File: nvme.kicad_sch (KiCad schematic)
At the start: 18 parts, among them J3 Bus_M.2_Socket_M, U1 ASEK-32.768KHZ-L-R-T, U2 AP3441SHE-7B

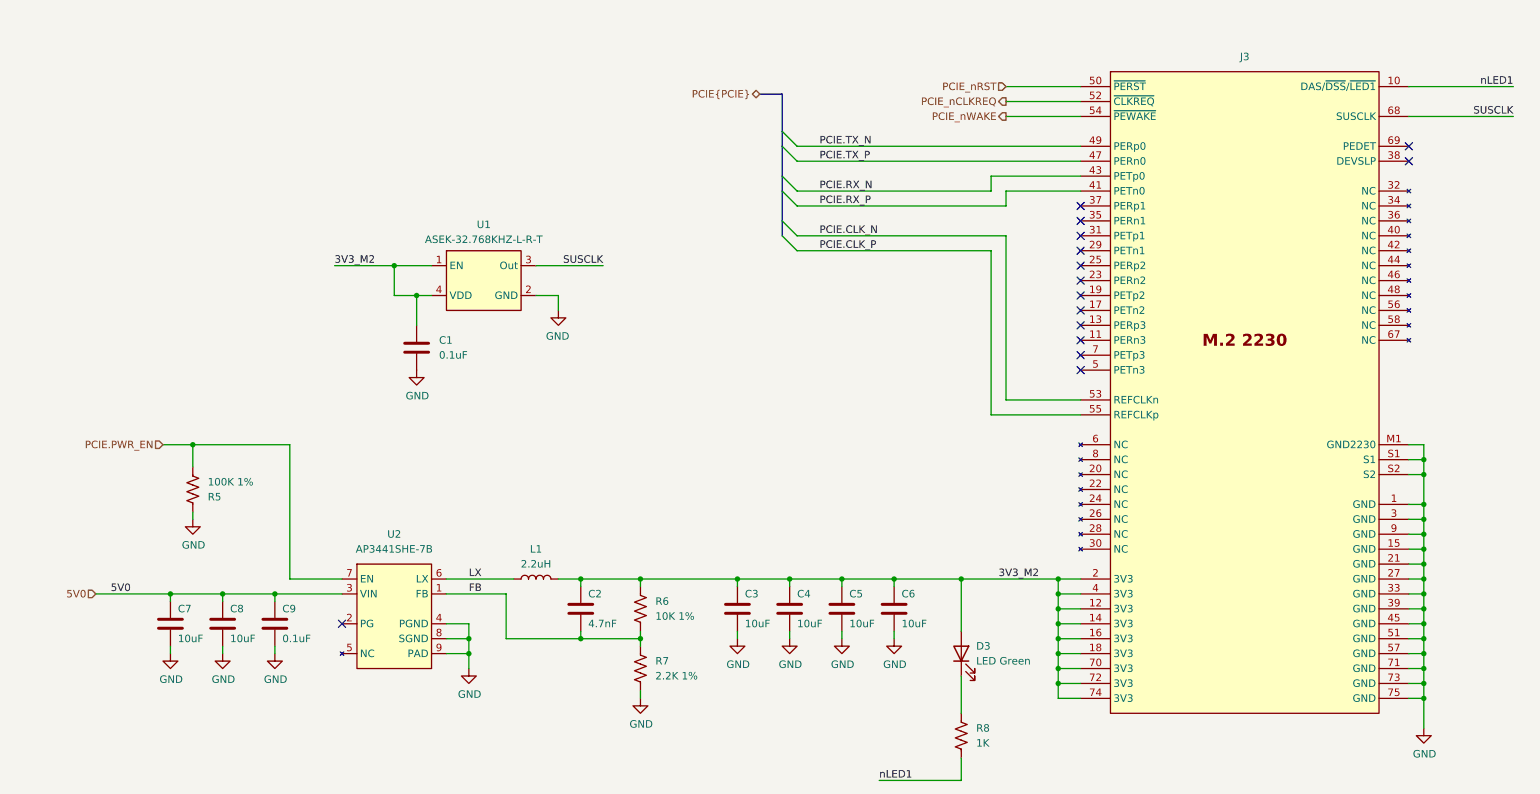
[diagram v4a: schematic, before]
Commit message: abstractified pcie sideband sigs
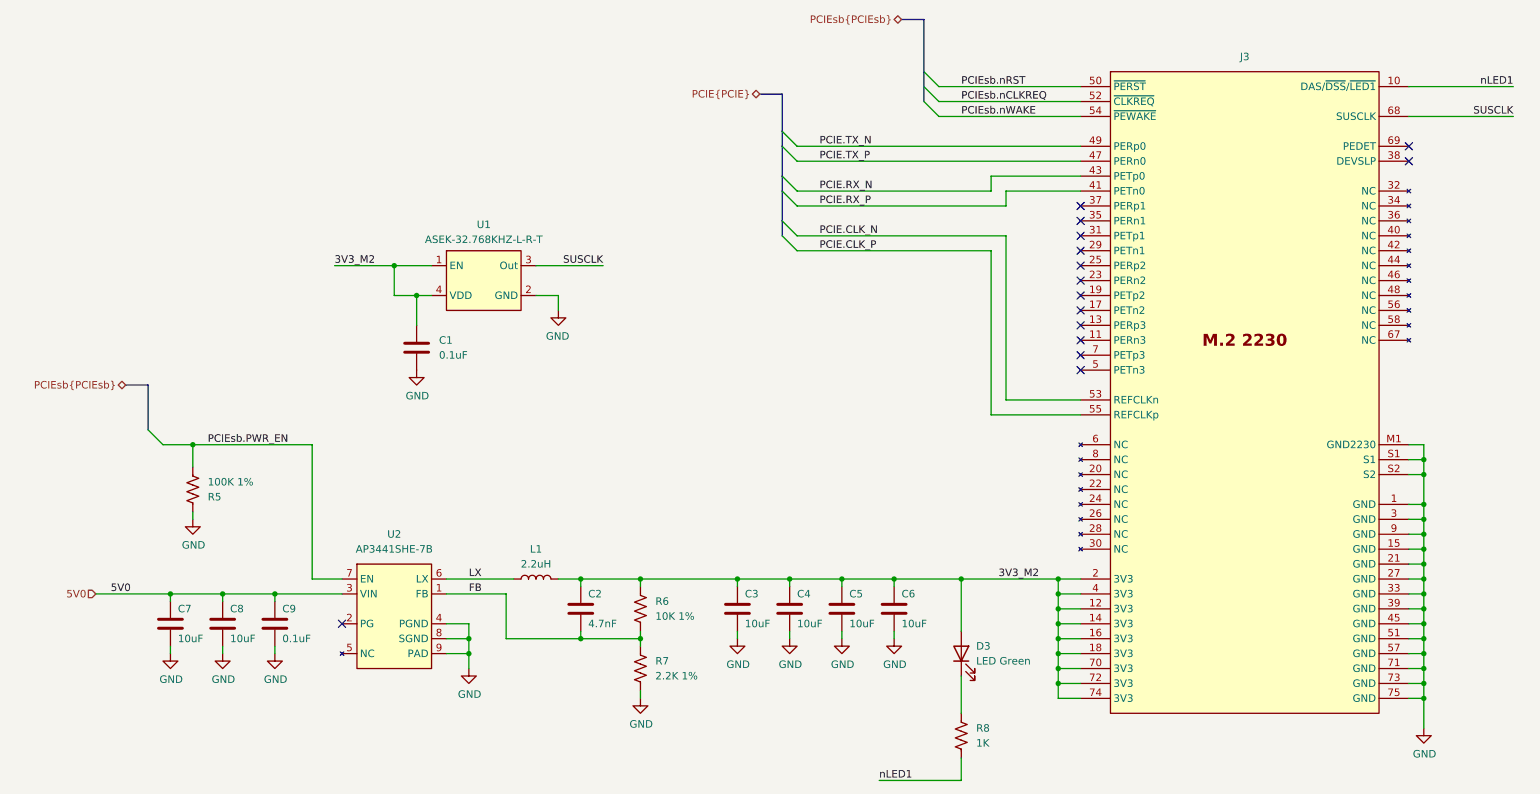
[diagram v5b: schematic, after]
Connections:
- net PCIE.PWR_EN renamed PCIEsb.PWR_EN
- net PCIE_nCLKREQ renamed PCIEsb.nCLKREQ
- net PCIE_nRST renamed PCIEsb.nRST
- net PCIE_nWAKE renamed PCIEsb.nWAKE
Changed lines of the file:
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@@
+	)
+	(bus_entry
+		(at 172.72 41.91)
+		(size -2.54 -2.54)
+		(stroke
+			(width 0)
+			(type default)
+		)
 	)
 	(bus_entry
@@
 	)
 	(bus_entry
+		(at 172.72 39.37)
+		(size -2.54 -2.54)
+		(stroke
+			(width 0)
+			(type default)
+		)
+	)
+	(bus_entry
 		(at 146.05 62.23)
 		(size 2.54 2.54)
+		(stroke
+			(width 0)
+			(type default)
+		)
+	)
+	(bus_entry
+		(at 172.72 36.83)
+		(size -2.54 -2.54)
 		(stroke
 			(width 0)
@@
 	)
 	(bus_entry
+		(at 38.1 95.25)
+		(size 2.54 2.54)
+		(stroke
+			(width 0)
+			(type default)
+		)
+	)
+	(bus_entry
 		(at 146.05 46.99)
 		(size 2.54 2.54)
@@
 		)
 	)
+	(bus
+		(pts
+			(xy 34.29 87.63) (xy 38.1 87.63)
+		)
+		(stroke
+			(width 0)
+			(type default)
+		)
+	)
 	(wire
 		(pts
@@
 	(wire
 		(pts
-			(xy 184.15 41.91) (xy 196.85 41.91)
+			(xy 172.72 41.91) (xy 196.85 41.91)
 		)
 		(stroke
@@
 		)
 	)
+	(bus
+		(pts
+			(xy 38.1 87.63) (xy 38.1 95.25)
+		)
+		(stroke
+			(width 0)
+			(type default)
+		)
+	)
 	(wire
 		(pts
@@
 		)
 	)
+	(bus
+		(pts
+			(xy 170.18 39.37) (xy 170.18 36.83)
+		)
+		(stroke
+			(width 0)
+			(type default)
+		)
+	)
 	(wire
 		(pts
@@
 		)
 	)
+	(bus
+		(pts
+			(xy 170.18 36.83) (xy 170.18 34.29)
+		)
+		(stroke
+			(width 0)
+			(type default)
+		)
+	)
 	(wire
 		(pts
@@
 	(wire
 		(pts
-			(xy 62.23 120.65) (xy 71.12 120.65)
+			(xy 66.04 120.65) (xy 71.12 120.65)
 		)
 		(stroke
@@
 	(wire
 		(pts
+			(xy 45.72 97.79) (xy 66.04 97.79)
+		)
+		(stroke
+			(width 0)
+			(type default)
+		)
+	)
+	(wire
+		(pts
 			(xy 255.27 125.73) (xy 255.27 128.27)
 		)
@@
 	(wire
 		(pts
-			(xy 45.72 97.79) (xy 62.23 97.79)
-		)
-		(stroke
-			(width 0)
-			(type default)
-		)
-	)
-	(wire
-		(pts
 			(xy 107.95 72.39) (xy 104.14 72.39)
 		)
@@
 	(wire
 		(pts
-			(xy 184.15 36.83) (xy 196.85 36.83)
+			(xy 172.72 36.83) (xy 196.85 36.83)
 		)
 		(stroke
@@
 		)
 	)
+	(bus
+		(pts
+			(xy 170.18 25.4) (xy 166.37 25.4)
+		)
+		(stroke
+			(width 0)
+			(type default)
+		)
+	)
 	(wire
 		(pts
@@
 		)
 	)
+	(bus
+		(pts
+			(xy 170.18 34.29) (xy 170.18 25.4)
+		)
+		(stroke
+			(width 0)
+			(type default)
+		)
+	)
 	(wire
 		(pts
@@
 	(wire
 		(pts
-			(xy 184.15 39.37) (xy 196.85 39.37)
-		)
-		(stroke
-			(width 0)
-			(type solid)
-		)
-	)
-	(wire
-		(pts
-			(xy 62.23 97.79) (xy 62.23 120.65)
+			(xy 172.72 39.37) (xy 196.85 39.37)
+		)
+		(stroke
+			(width 0)
+			(type solid)
+		)
+	)
+	(wire
+		(pts
+			(xy 66.04 97.79) (xy 66.04 120.65)
 		)
 		(stroke
@@
 		)
 	)
+	(label "PCIEsb.PWR_EN"
+		(at 48.26 97.79 0)
+		(effects
+			(font
+				(size 1.27 1.27)
+			)
+			(justify left bottom)
+		)
+	)
 	(label "5V0"
 		(at 31.75 123.19 0)
@@
 		)
 	)
+	(label "PCIEsb.nWAKE"
+		(at 176.53 41.91 0)
+		(effects
+			(font
+				(size 1.27 1.27)
+			)
+			(justify left bottom)
+		)
+	)
 	(label "PCIE.CLK_P"
 		(at 152.4 64.77 0)
@@
 		)
 	)
+	(label "PCIEsb.nCLKREQ"
+		(at 176.53 39.37 0)
+		(effects
+			(font
+				(size 1.27 1.27)
+			)
+			(justify left bottom)
+		)
+	)
 	(label "nLED1"
 		(at 162.56 154.94 0)
@@
 	(label "PCIE.RX_P"
 		(at 152.4 57.15 0)
+		(effects
+			(font
+				(size 1.27 1.27)
+			)
+			(justify left bottom)
+		)
+	)
+	(label "PCIEsb.nRST"
+		(at 176.53 36.83 0)
 		(effects
 			(font
@@
 		)
 	)
-	(hierarchical_label "PCIE.PWR_EN"
-		(shape input)
-		(at 40.64 97.79 180)
-		(effects
-			(font
-				(size 1.27 1.27)
-			)
-			(justify right)
-		)
-	)
-	(hierarchical_label "PCIE_nRST"
-		(shape input)
-		(at 184.15 36.83 180)
+	(hierarchical_label "PCIEsb{PCIEsb}"
+		(shape bidirectional)
+		(at 166.37 25.4 180)
 		(effects
 			(font
@@
 		)
 	)
-	(hierarchical_label "PCIE_nWAKE"
-		(shape output)
-		(at 184.15 41.91 180)
-		(effects
-			(font
-				(size 1.27 1.27)
-			)
-			(justify right)
-		)
-	)
-	(hierarchical_label "PCIE_nCLKREQ"
-		(shape output)
-		(at 184.15 39.37 180)
-		(effects
-			(font
+	(hierarchical_label "PCIEsb{PCIEsb}"
+		(shape bidirectional)
+		(at 34.29 87.63 180)
+		(effects
+			(font

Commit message: neo m8m impl.
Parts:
- added 3V3_M2: TestPoint, TestPoint:TestPoint_Pad_D1.0mm, symbol Connector:TestPoint
- renumbered C7 to C1, C8 to C2, C9 to C3, C1 to C4, C2 to C5, C3 to C6, C4 to C7, C5 to C8, C6 to C9, U2 to U1, U1 to U2
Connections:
- net 3V3_M2: now also 3V3_M2.1
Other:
- moved on the sheet: C1, C2, C3, C4, C5, C6, C7, C8, C9, D3, J3, L1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

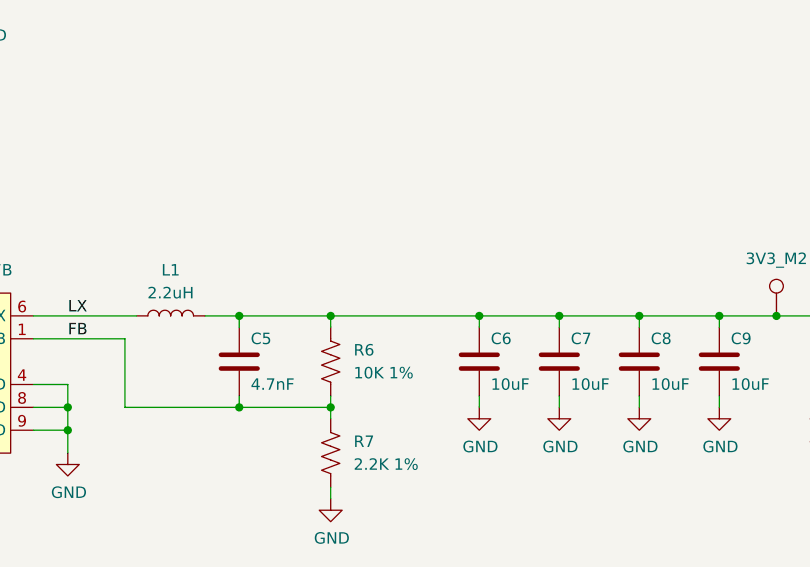
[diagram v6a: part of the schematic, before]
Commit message: prepared usb3, abstracted cameras, backplane connector
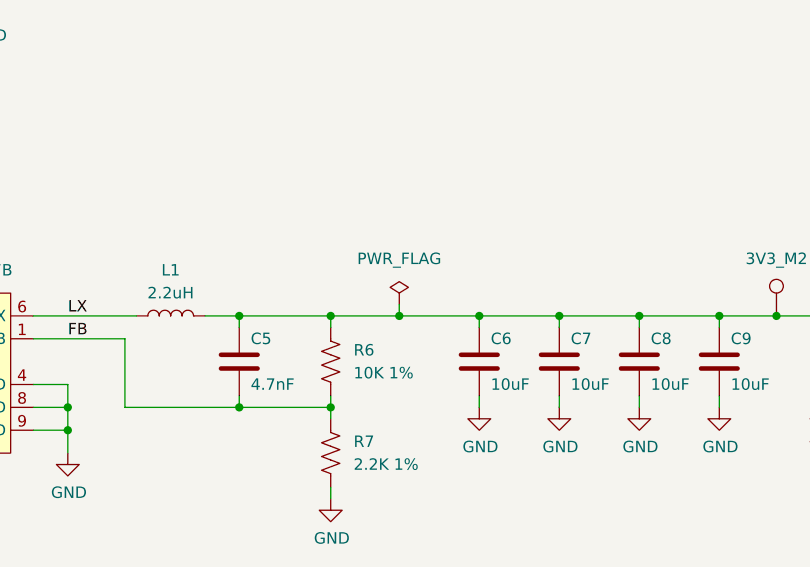
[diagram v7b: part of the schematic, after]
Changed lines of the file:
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@@
 	(title_block
 		(title "CUTIE-CITRUS PCB")
-		(date "2025-11-24")
+		(date "2025-12-11")
 		(rev "A")
 		(company "Andre S Winkel | Highlander Space Program | University of California, Riverside")
@@
 	(junction
 		(at 195.58 138.43)
+		(diameter 0)
+		(color 255 0 255 1)
+	)
+	(junction
+		(at 132.08 120.65)
 		(diameter 0)
 		(color 255 0 255 1)
@@
 	(wire
 		(pts
+			(xy 132.08 120.65) (xy 140.97 120.65)
+		)
+		(stroke
+			(width 0.381)
+			(type default)
+			(color 255 0 255 1)
+		)
+	)
+	(wire
+		(pts
 			(xy 257.81 102.87) (xy 255.27 102.87)
 		)
@@
 	(wire
 		(pts
+			(xy 132.08 119.38) (xy 132.08 120.65)
+		)
+		(stroke
+			(width 0.381)
+			(type default)
+			(color 255 0 255 1)
+		)
+	)
+	(wire
+		(pts
 			(xy 165.1 154.94) (xy 179.07 154.94)
 		)
@@
 	(wire
 		(pts
-			(xy 124.46 120.65) (xy 140.97 120.65)
+			(xy 124.46 120.65) (xy 132.08 120.65)
 		)
 		(stroke
@@
 					(unit 1)
 				)
+			)
+		)
+	)
+	(symbol
+		(lib_id "power:PWR_FLAG")
+		(at 132.08 119.38 0)
+		(unit 1)
+		(exclude_from_sim no)
+		(in_bom yes)
+		(on_board yes)
+		(dnp no)
+		(fields_autoplaced yes)
+		(property "Reference" "#FLG03"
+			(at 132.08 117.475 0)
+			(effects
+				(font
+					(size 1.27 1.27)
+				)
+				(hide yes)
+			)
+		)
+		(property "Value" "PWR_FLAG"
+			(at 132.08 114.3 0)
+			(effects
+				(font
+					(size 1.27 1.27)
+				)
+			)
+		)
+		(property "Footprint" ""
+			(at 132.08 119.38 0)
+			(effects
+				(font
+					(size 1.27 1.27)
+				)
+				(hide yes)
+			)
+		)
+		(property "Datasheet" "~"
+			(at 132.08 119.38 0)
+			(effects
+				(font
+					(size 1.27 1.27)
+				)
+				(hide yes)
+			)
+		)
+		(property "Description" "Special symbol for telling ERC where power comes from"
+			(at 132.08 119.38 0)
+			(effects
+				(font
+					(size 1.27 1.27)
+				)
+				(hide yes)
+			)
+		)
+		(pin "1"
+		)
+		(instances
+			(project ""
+				(path "/40af415e-5e3a-41a5-ab07-08c2181863e4/7953df6c-8185-4fff-8cd2-b6d3791adbaa"
+					(reference "#FLG03")
+					(unit 1)
+				)

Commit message: un-abstraction, footprints, layout edge cuts
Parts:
- L1: footprint CM5IO:L_Bourns_SRP5030CC -> Capacitor_SMD:C_0402_1005Metric
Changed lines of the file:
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@@
 			)
 		)
-		(property "Footprint" "CM5IO:L_Bourns_SRP5030CC"
+		(property "Footprint" "Capacitor_SMD:C_0402_1005Metric"
 			(at 106.68 120.65 0)
 			(effects
